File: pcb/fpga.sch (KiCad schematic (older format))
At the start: 29 parts, among them J1 CONN_INTEGRALSTICK_FPGA_DEVICE, Q1 SSM6N58NU, Q2 SSM6N58NU, Q3 SSM6N58NU, U12 DSC6001HI2A-025.0000‎, U2 XC7A50T-1FTG256C, U9 AT24MAC402-UDFN

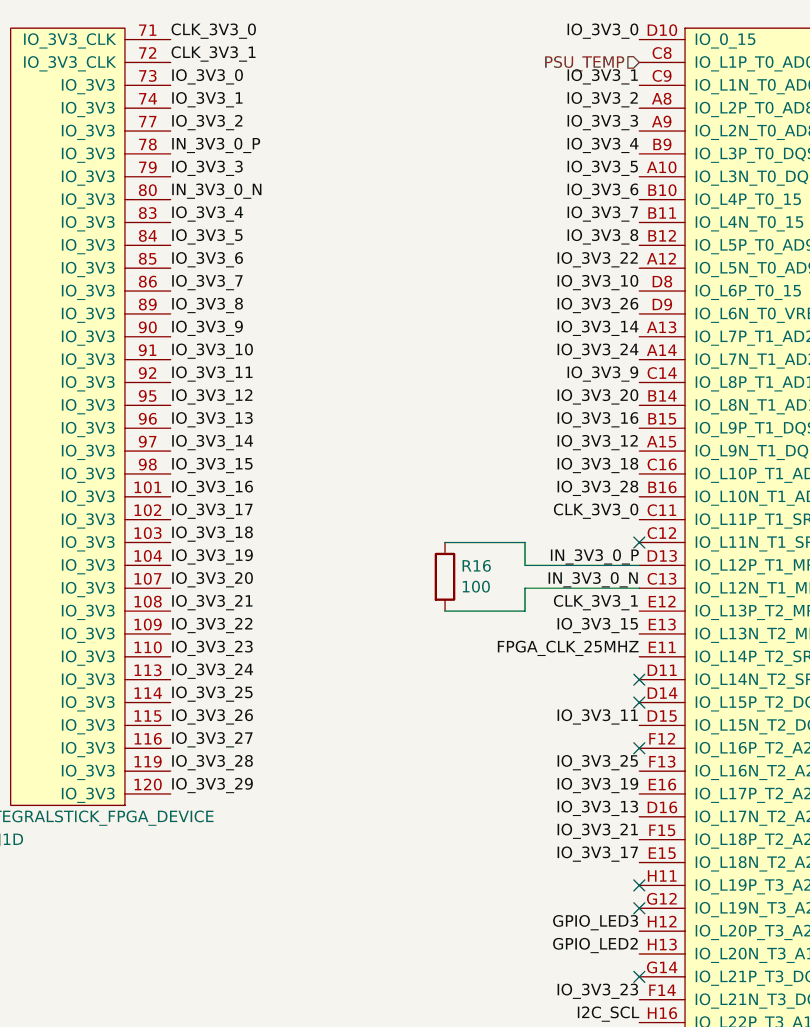
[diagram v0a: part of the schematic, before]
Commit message: Continued routing 3.3V GPIO bus. Everything that can be fanned out on top metal is done.
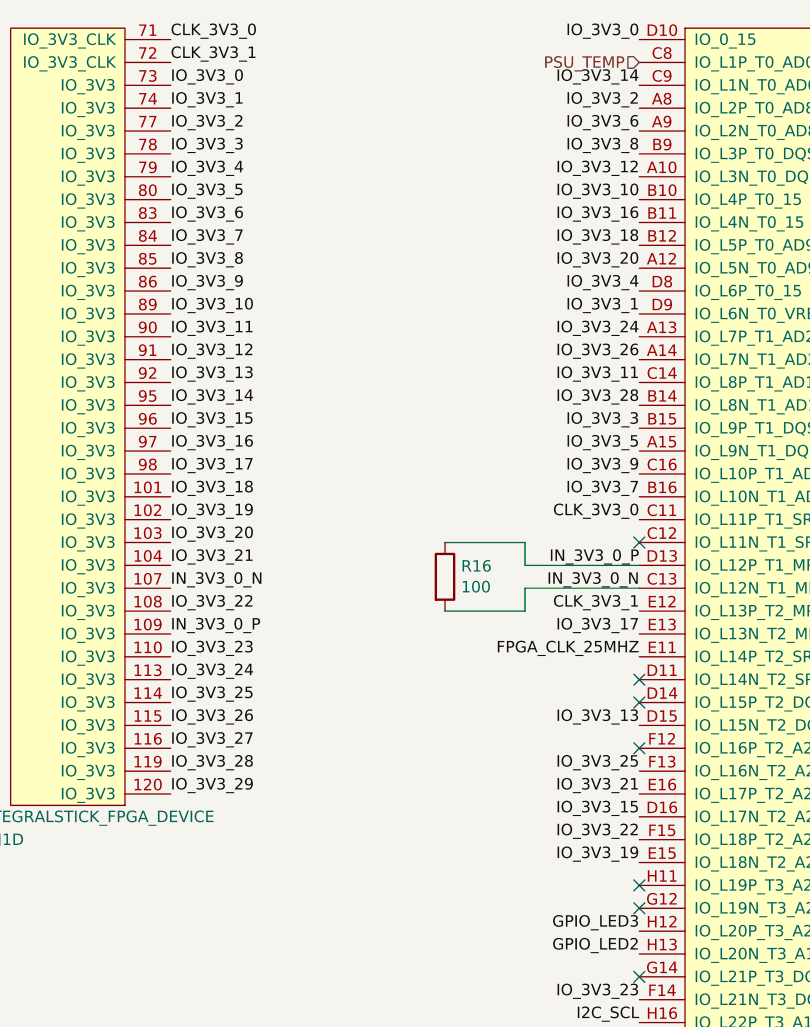
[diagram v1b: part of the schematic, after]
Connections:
- net IN_3V3_0_N: now also J1.107 (IO_3V3); no longer J1.80 (IO_3V3)
- net IN_3V3_0_P: now also J1.109 (IO_3V3); no longer J1.78 (IO_3V3)
- net IO_3V3_1: now also U2.D9 (IO_L6N_T0_VREF_15); no longer U2.C9 (IO_L1N_T0_AD0N_15)
- net IO_3V3_10: now also J1.89 (IO_3V3), U2.B10 (IO_L4P_T0_15); no longer J1.91 (IO_3V3), U2.D8 (IO_L6P_T0_15)
- net IO_3V3_11: now also J1.90 (IO_3V3), U2.C14 (IO_L8P_T1_AD10P_15); no longer J1.92 (IO_3V3), U2.D15 (IO_L15N_T2_DQS_ADV_B_15)
- net IO_3V3_12: now also J1.91 (IO_3V3), U2.A10 (IO_L3N_T0_DQS_AD1N_15); no longer J1.95 (IO_3V3), U2.A15 (IO_L9N_T1_DQS_AD3N_15)
- net IO_3V3_13: now also J1.92 (IO_3V3), U2.D15 (IO_L15N_T2_DQS_ADV_B_15); no longer J1.96 (IO_3V3), U2.D16 (IO_L17N_T2_A25_15)
- net IO_3V3_14: now also J1.95 (IO_3V3), U2.C9 (IO_L1N_T0_AD0N_15); no longer J1.97 (IO_3V3), U2.A13 (IO_L7P_T1_AD2P_15)
- net IO_3V3_15: now also J1.96 (IO_3V3), U2.D16 (IO_L17N_T2_A25_15); no longer J1.98 (IO_3V3), U2.E13 (IO_L13N_T2_MRCC_15)
- net IO_3V3_16: now also J1.97 (IO_3V3), U2.B11 (IO_L4N_T0_15); no longer J1.101 (IO_3V3), U2.B15 (IO_L9P_T1_DQS_AD3P_15)
- net IO_3V3_17: now also J1.98 (IO_3V3), U2.E13 (IO_L13N_T2_MRCC_15); no longer J1.102 (IO_3V3), U2.E15 (IO_L18N_T2_A23_15)
- net IO_3V3_18: now also J1.101 (IO_3V3), U2.B12 (IO_L5P_T0_AD9P_15); no longer J1.103 (IO_3V3), U2.C16 (IO_L10P_T1_AD11P_15)
- net IO_3V3_19: now also J1.102 (IO_3V3), U2.E15 (IO_L18N_T2_A23_15); no longer J1.104 (IO_3V3), U2.E16 (IO_L17P_T2_A26_15)
- net IO_3V3_20: now also J1.103 (IO_3V3), U2.A12 (IO_L5N_T0_AD9N_15); no longer J1.107 (IO_3V3), U2.B14 (IO_L8N_T1_AD10N_15)
- net IO_3V3_21: now also J1.104 (IO_3V3), U2.E16 (IO_L17P_T2_A26_15); no longer J1.108 (IO_3V3), U2.F15 (IO_L18P_T2_A24_15)
- net IO_3V3_22: now also J1.108 (IO_3V3), U2.F15 (IO_L18P_T2_A24_15); no longer J1.109 (IO_3V3), U2.A12 (IO_L5N_T0_AD9N_15)
- net IO_3V3_24: now also U2.A13 (IO_L7P_T1_AD2P_15); no longer U2.A14 (IO_L7N_T1_AD2N_15)
- net IO_3V3_26: now also U2.A14 (IO_L7N_T1_AD2N_15); no longer U2.D9 (IO_L6N_T0_VREF_15)
- net IO_3V3_28: now also U2.B14 (IO_L8N_T1_AD10N_15); no longer U2.B16 (IO_L10N_T1_AD11N_15)
- net IO_3V3_3: now also J1.78 (IO_3V3), U2.B15 (IO_L9P_T1_DQS_AD3P_15); no longer J1.79 (IO_3V3), U2.A9 (IO_L2N_T0_AD8N_15)
- net IO_3V3_4: now also J1.79 (IO_3V3), U2.D8 (IO_L6P_T0_15); no longer J1.83 (IO_3V3), U2.B9 (IO_L3P_T0_DQS_AD1P_15)
- net IO_3V3_5: now also J1.80 (IO_3V3), U2.A15 (IO_L9N_T1_DQS_AD3N_15); no longer J1.84 (IO_3V3), U2.A10 (IO_L3N_T0_DQS_AD1N_15)
- net IO_3V3_6: now also J1.83 (IO_3V3), U2.A9 (IO_L2N_T0_AD8N_15); no longer J1.85 (IO_3V3), U2.B10 (IO_L4P_T0_15)
- net IO_3V3_7: now also J1.84 (IO_3V3), U2.B16 (IO_L10N_T1_AD11N_15); no longer J1.86 (IO_3V3), U2.B11 (IO_L4N_T0_15)
- net IO_3V3_8: now also J1.85 (IO_3V3), U2.B9 (IO_L3P_T0_DQS_AD1P_15); no longer J1.89 (IO_3V3), U2.B12 (IO_L5P_T0_AD9P_15)
- net IO_3V3_9: now also J1.86 (IO_3V3), U2.C16 (IO_L10P_T1_AD11P_15); no longer J1.90 (IO_3V3), U2.C14 (IO_L8P_T1_AD10P_15)
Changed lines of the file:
@@
 Text Label 6350 1150 0    50   ~ 0
 IO_3V3_2
-Text Label 6350 1350 0    50   ~ 0
+Text Label 6350 1250 0    50   ~ 0
 IO_3V3_3
 Text Label 6350 750  0    50   ~ 0
@@
 Text Label 6350 850  0    50   ~ 0
 CLK_3V3_1
+Text Label 6350 1350 0    50   ~ 0
+IO_3V3_4
+Text Label 6350 1450 0    50   ~ 0
+IO_3V3_5
 Text Label 6350 1550 0    50   ~ 0
-IO_3V3_4
+IO_3V3_6
 Text Label 6350 1650 0    50   ~ 0
-IO_3V3_5
+IO_3V3_7
 Text Label 6350 1750 0    50   ~ 0
-IO_3V3_6
+IO_3V3_8
 Text Label 6350 1850 0    50   ~ 0
-IO_3V3_7
+IO_3V3_9
 Text Label 6350 1950 0    50   ~ 0
-IO_3V3_8
+IO_3V3_10
 Text Label 6350 2050 0    50   ~ 0
-IO_3V3_9
+IO_3V3_11
 Text Label 6350 2150 0    50   ~ 0
-IO_3V3_10
+IO_3V3_12
 Text Label 6350 2250 0    50   ~ 0
-IO_3V3_11
+IO_3V3_13
 Text Label 6350 2350 0    50   ~ 0
-IO_3V3_12
+IO_3V3_14
 Text Label 6350 2450 0    50   ~ 0
-IO_3V3_13
+IO_3V3_15
 Text Label 6350 2550 0    50   ~ 0
-IO_3V3_14
+IO_3V3_16
 Text Label 6350 2650 0    50   ~ 0
-IO_3V3_15
+IO_3V3_17
 Text Label 6350 2750 0    50   ~ 0
-IO_3V3_16
+IO_3V3_18
 Text Label 6350 2850 0    50   ~ 0
-IO_3V3_17
+IO_3V3_19
 Text Label 6350 2950 0    50   ~ 0
-IO_3V3_18
+IO_3V3_20
 Text Label 6350 3050 0    50   ~ 0
-IO_3V3_19
-Text Label 6350 3150 0    50   ~ 0
-IO_3V3_20
+IO_3V3_21
 Text Label 6350 3250 0    50   ~ 0
-IO_3V3_21
-Text Label 6350 3350 0    50   ~ 0
 IO_3V3_22
 Text Label 6350 3450 0    50   ~ 0
@@
 Text Label 8400 750  2    50   ~ 0
 IO_3V3_0
-Text Label 8400 950  2    50   ~ 0
+Text Label 8400 1950 2    50   ~ 0
 IO_3V3_1
 Text Label 8400 1050 2    50   ~ 0
 IO_3V3_2
-Text Label 8400 1150 2    50   ~ 0
+Text Label 8400 2450 2    50   ~ 0
 IO_3V3_3
 Text Label 8400 2850 2    50   ~ 0
@@
 Text Label 8400 3250 2    50   ~ 0
 CLK_3V3_1
+Text Label 8400 1850 2    50   ~ 0
+IO_3V3_4
+Text Label 8400 2550 2    50   ~ 0
+IO_3V3_5
+Text Label 8400 1150 2    50   ~ 0
+IO_3V3_6
+Text Label 8400 2750 2    50   ~ 0
+IO_3V3_7
 Text Label 8400 1250 2    50   ~ 0
-IO_3V3_4
+IO_3V3_8
+Text Label 8400 2650 2    50   ~ 0
+IO_3V3_9
+Text Label 8400 1450 2    50   ~ 0
+IO_3V3_10
+Text Label 8400 2250 2    50   ~ 0
+IO_3V3_11
 Text Label 8400 1350 2    50   ~ 0
-IO_3V3_5
-Text Label 8400 1450 2    50   ~ 0
-IO_3V3_6
+IO_3V3_12
+Text Label 8400 3750 2    50   ~ 0
+IO_3V3_13
+Text Label 8400 950  2    50   ~ 0
+IO_3V3_14
+Text Label 8400 4150 2    50   ~ 0
+IO_3V3_15
 Text Label 8400 1550 2    50   ~ 0
-IO_3V3_7
+IO_3V3_16
+Text Label 8400 3350 2    50   ~ 0
+IO_3V3_17
 Text Label 8400 1650 2    50   ~ 0
-IO_3V3_8
-Text Label 8400 2250 2    50   ~ 0
-IO_3V3_9
-Text Label 8400 1850 2    50   ~ 0
-IO_3V3_10
-Text Label 8400 3750 2    50   ~ 0
-IO_3V3_11
-Text Label 8400 2550 2    50   ~ 0
-IO_3V3_12
-Text Label 8400 4150 2    50   ~ 0
-IO_3V3_13
-Text Label 8400 2050 2    50   ~ 0
-IO_3V3_14
-Text Label 8400 3350 2    50   ~ 0
-IO_3V3_15
-Text Label 8400 2450 2    50   ~ 0
-IO_3V3_16
+IO_3V3_18
 Text Label 8400 4350 2    50   ~ 0
-IO_3V3_17
-Text Label 8400 2650 2    50   ~ 0
-IO_3V3_18
+IO_3V3_19
+Text Label 8400 1750 2    50   ~ 0
+IO_3V3_20
 Text Label 8400 4050 2    50   ~ 0
-IO_3V3_19
-Text Label 8400 2350 2    50   ~ 0
-IO_3V3_20
+IO_3V3_21
 Text Label 8400 4250 2    50   ~ 0
-IO_3V3_21
-Text Label 8400 1750 2    50   ~ 0
 IO_3V3_22
 Text Label 8400 4950 2    50   ~ 0
 IO_3V3_23
-Text Label 8400 2150 2    50   ~ 0
+Text Label 8400 2050 2    50   ~ 0
 IO_3V3_24
 Text Label 8400 3950 2    50   ~ 0
 IO_3V3_25
-Text Label 8400 1950 2    50   ~ 0
+Text Label 8400 2150 2    50   ~ 0
 IO_3V3_26
 Text Label 8400 5150 2    50   ~ 0
 IO_3V3_27
-Text Label 8400 2750 2    50   ~ 0
+Text Label 8400 2350 2    50   ~ 0
 IO_3V3_28
 Text Label 8400 5550 2    50   ~ 0
@@
 Wire Wire Line
 	7900 3250 7550 3250
-Text Label 6350 1250 0    50   ~ 0
+Text Label 6350 3350 0    50   ~ 0
 IN_3V3_0_P
-Text Label 6350 1450 0    50   ~ 0
+Text Label 6350 3150 0    50   ~ 0
 IN_3V3_0_N
 NoConn ~ 13900 3450

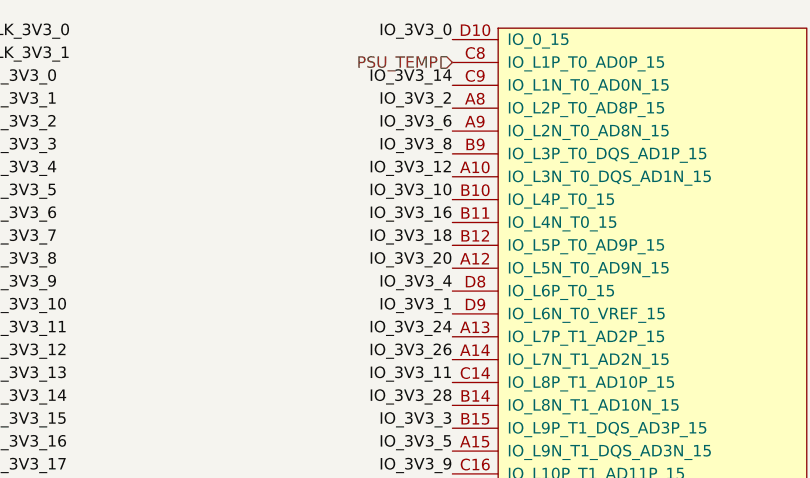
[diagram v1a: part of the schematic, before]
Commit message: Finished routing 3.3V GPIO bus
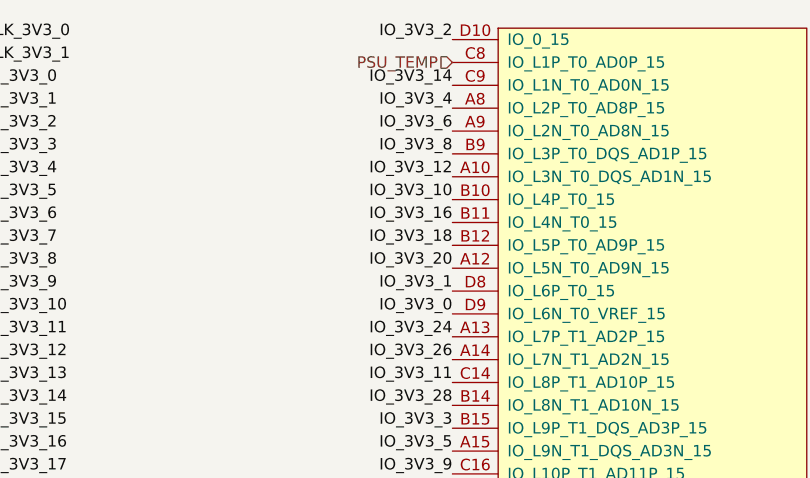
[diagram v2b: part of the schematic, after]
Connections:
- net IO_3V3_0: now also U2.D9 (IO_L6N_T0_VREF_15); no longer U2.D10 (IO_0_15)
- net IO_3V3_1: now also U2.D8 (IO_L6P_T0_15); no longer U2.D9 (IO_L6N_T0_VREF_15)
- net IO_3V3_2: now also U2.D10 (IO_0_15); no longer U2.A8 (IO_L2P_T0_AD8P_15)
- net IO_3V3_4: now also U2.A8 (IO_L2P_T0_AD8P_15); no longer U2.D8 (IO_L6P_T0_15)
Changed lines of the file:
@@
 Text Label 6350 4050 0    50   ~ 0
 IO_3V3_29
+Text Label 8400 1950 2    50   ~ 0
+IO_3V3_0
+Text Label 8400 1850 2    50   ~ 0
+IO_3V3_1
 Text Label 8400 750  2    50   ~ 0
-IO_3V3_0
-Text Label 8400 1950 2    50   ~ 0
-IO_3V3_1
-Text Label 8400 1050 2    50   ~ 0
 IO_3V3_2
 Text Label 8400 2450 2    50   ~ 0
@@
 Text Label 8400 3250 2    50   ~ 0
 CLK_3V3_1
-Text Label 8400 1850 2    50   ~ 0
+Text Label 8400 1050 2    50   ~ 0
 IO_3V3_4
 Text Label 8400 2550 2    50   ~ 0
